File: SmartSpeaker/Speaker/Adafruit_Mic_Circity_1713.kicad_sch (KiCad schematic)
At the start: 17 parts, among them J2 HEADER-1X576MIL, Q1 CMA-4544PF-W

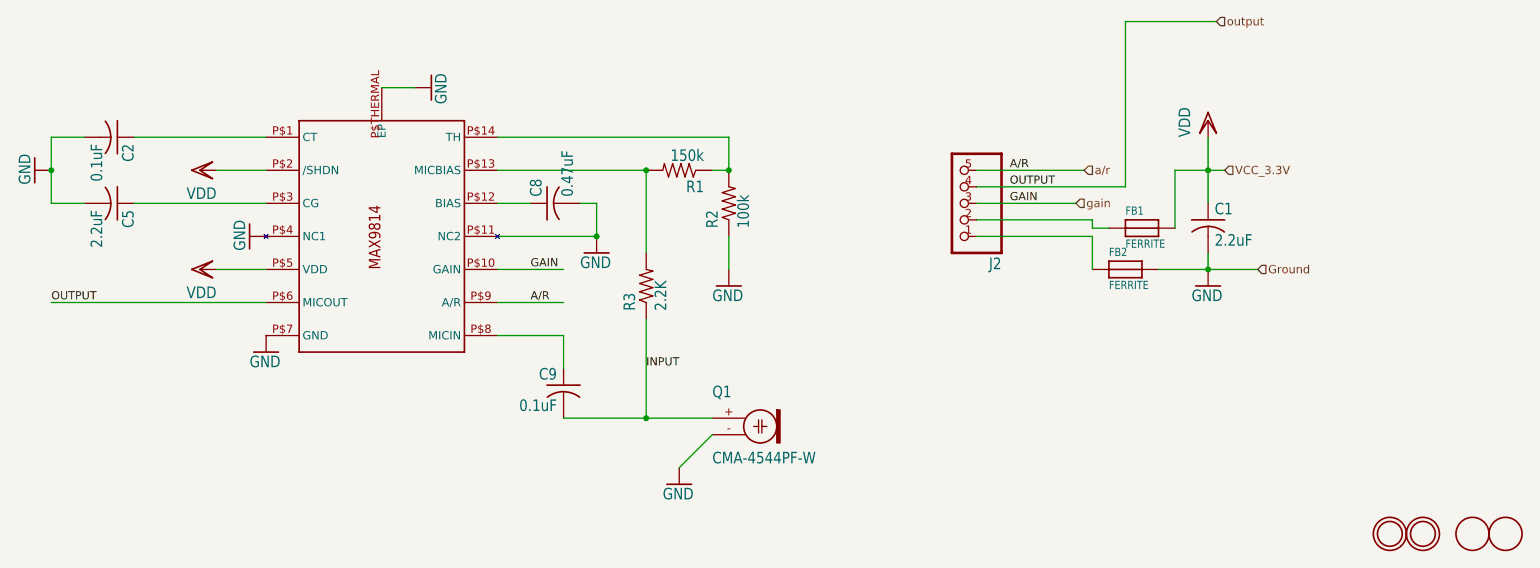
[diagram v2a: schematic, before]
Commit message: Fix some footprint problems, work towards a PCB
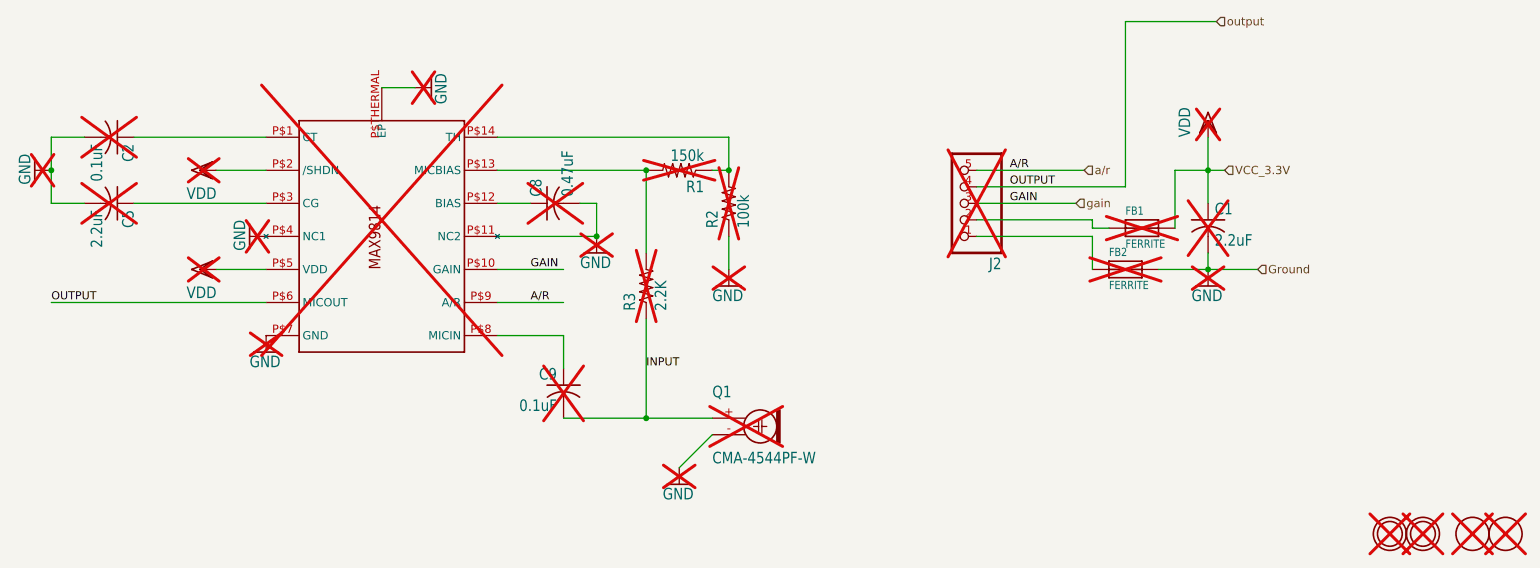
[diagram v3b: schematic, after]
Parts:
- C1, C2, C5, C8, C9, FB1, FB2, J2, Q1, R1, R2, R3, U$1, U$2, U$3, U$4, U$5: now not fitted
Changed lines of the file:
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@@
 		(in_bom yes)
 		(on_board no)
-		(dnp no)
+		(dnp yes)
 		(property "Reference" "R1"
 			(at 137.16 105.6386 0)
@@
 		(in_bom yes)
 		(on_board no)
-		(dnp no)
+		(dnp yes)
 		(property "Reference" "FB1"
 			(at 201.93 111.125 0)
@@
 		(in_bom yes)
 		(on_board no)
-		(dnp no)
+		(dnp yes)
 		(property "Reference" "#GND12"
 			(at 120.65 116.84 0)
@@
 		(in_bom yes)
 		(on_board no)
-		(dnp no)
+		(dnp yes)
 		(property "Reference" "R3"
 			(at 126.7714 125.73 0)
@@
 		(in_bom yes)
 		(on_board no)
-		(dnp no)
+		(dnp yes)
 		(property "Reference" "#GND9"
 			(at 140.97 121.92 0)
@@
 		(in_bom yes)
 		(on_board no)
-		(dnp no)
+		(dnp yes)
 		(property "Reference" "C1"
 			(at 215.646 111.125 0)
@@
 		(in_bom yes)
 		(on_board yes)
-		(dnp no)
+		(dnp yes)
 		(property "Reference" "#GND5"
 			(at 133.35 152.4 0)
@@
 		(in_bom yes)
 		(on_board no)
-		(dnp no)
+		(dnp yes)
 		(property "Reference" "#GND6"
 			(at 67.31 114.3 0)
@@
 		(in_bom yes)
 		(on_board no)
-		(dnp no)
+		(dnp yes)
 		(property "Reference" "R2"
 			(at 139.4714 113.03 0)
@@
 		(in_bom yes)
 		(on_board no)
-		(dnp no)
+		(dnp yes)
 		(property "Reference" "C8"
 			(at 112.395 108.204 0)
@@
 		(in_bom yes)
 		(on_board no)
-		(dnp no)
+		(dnp yes)
 		(property "Reference" "#GND2"
 			(at 95.25 91.44 0)
@@
 		(in_bom yes)
 		(on_board no)
-		(dnp no)
+		(dnp yes)
 		(property "Reference" "C5"
 			(at 47.625 110.236 0)
@@
 		(in_bom yes)
 		(on_board no)
-		(dnp no)
+		(dnp yes)
 		(property "Reference" "#VDD1"
 			(at 214.63 96.52 0)
@@
 		(in_bom yes)
 		(on_board no)
-		(dnp no)
+		(dnp yes)
 		(property "Reference" "J2"
 			(at 182.88 117.475 0)
@@
 		(in_bom yes)
 		(on_board no)
-		(dnp no)
+		(dnp yes)
 		(property "Reference" "#VDD8"
 			(at 59.69 119.38 0)
@@
 		(in_bom yes)
 		(on_board no)
-		(dnp no)
+		(dnp yes)
 		(property "Reference" "FB2"
 			(at 199.39 117.475 0)
@@
 		(in_bom yes)
 		(on_board no)
-		(dnp no)
+		(dnp yes)
 		(property "Reference" "U$1"
 			(at 85.09 134.62 0)
@@
 		(in_bom yes)
 		(on_board no)
-		(dnp no)
+		(dnp yes)
 		(property "Reference" "#VDD9"
 			(at 59.69 104.14 0)
@@
 		(in_bom yes)
 		(on_board no)
-		(dnp no)
+		(dnp yes)
 		(property "Reference" "Q1"
 			(at 138.43 137.16 0)
@@
 		(in_bom yes)
 		(on_board yes)
-		(dnp no)
+		(dnp yes)
 		(property "Reference" "#GND8"
 			(at 34.29 104.14 0)
@@
 		(in_bom yes)
 		(on_board no)
-		(dnp no)
+		(dnp yes)
 		(property "Reference" "#GND10"
 			(at 69.85 132.08 0)
@@
 		(in_bom yes)
 		(on_board yes)
-		(dnp no)
+		(dnp yes)
 		(property "Reference" "U$3"
 			(at 255.27 160.02 0)
@@
 		(in_bom yes)
 		(on_board no)
-		(dnp no)
+		(dnp yes)
 		(property "Reference" "C9"
 			(at 114.554 136.525 0)
@@
 		(in_bom yes)
 		(on_board yes)
-		(dnp no)
+		(dnp yes)
 		(property "Reference" "U$4"
 			(at 247.65 160.02 0)
@@
 		(in_bom yes)
 		(on_board yes)
-		(dnp no)
+		(dnp yes)
 		(property "Reference" "U$5"
 			(at 242.57 160.02 0)
@@
 		(in_bom yes)
 		(on_board no)
-		(dnp no)
+		(dnp yes)
 		(property "Reference" "#GND1"
 			(at 214.63 121.92 0)
@@
 		(in_bom yes)
 		(on_board yes)
-		(dnp no)
+		(dnp yes)
 		(property "Reference" "U$2"
 			(at 260.35 160.02 0)
@@
 		(in_bom yes)
 		(on_board no)
-		(dnp no)
+		(dnp yes)
 		(property "Reference" "C2"
 			(at 47.625 100.076 0)

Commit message: Edit PCB to fix issues: - Enlarge OSHW logo - Rotate footprints for screw terminals - Fix pad numbers for barrel jack
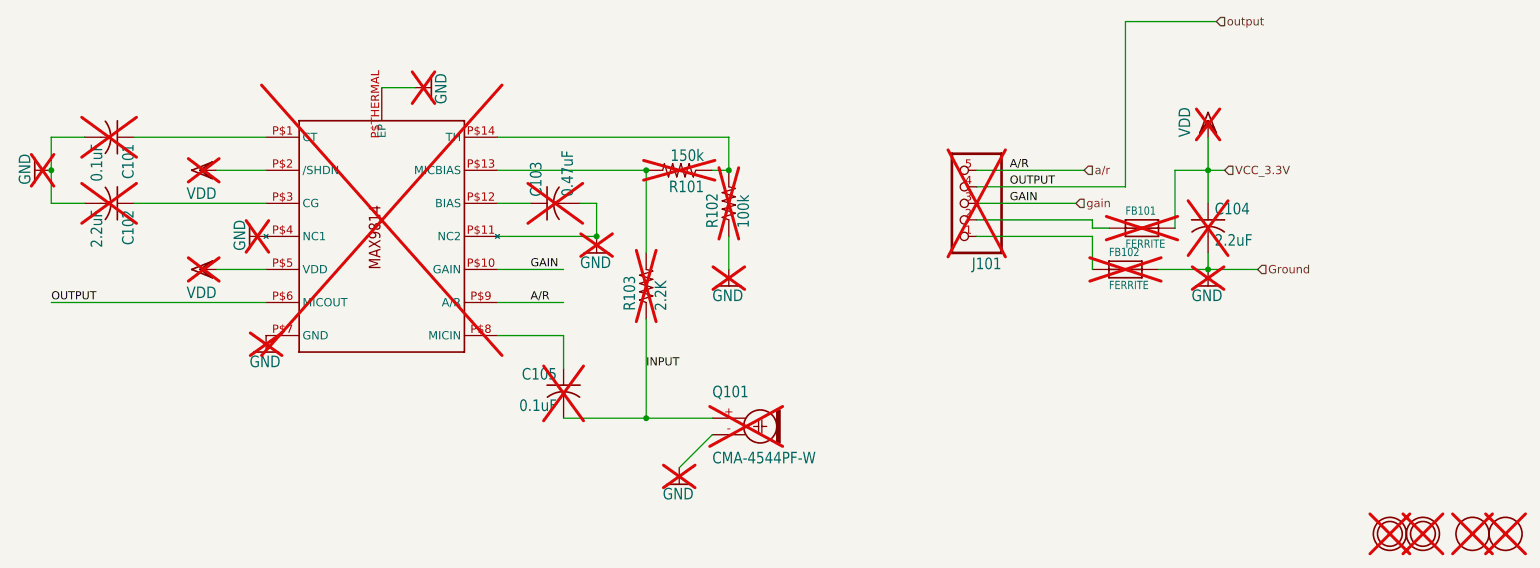
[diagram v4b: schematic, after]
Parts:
- renumbered C2 to C101, C5 to C102, C8 to C103, C1 to C104, C9 to C105, FB1 to FB101, FB2 to FB102, J2 to J101, Q1 to Q101, R1 to R101, R2 to R102, R3 to R103, U$1 to U$101, U$5 to U$102, U$4 to U$103, U$3 to U$104, U$2 to U$105
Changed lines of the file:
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@@
 (kicad_sch
-	(version 20231120)
+	(version 20250114)
 	(generator "eeschema")
-	(generator_version "8.0")
+	(generator_version "9.0")
 	(paper "A4")
 	(junction
@@
 		(on_board no)
 		(dnp yes)
-		(property "Reference" "R1"
+		(property "Reference" "R101"
 			(at 137.16 105.6386 0)
 			(effects
@@
 		(on_board no)
 		(dnp yes)
-		(property "Reference" "FB1"
+		(property "Reference" "FB101"
 			(at 201.93 111.125 0)
 			(effects
@@
 		(on_board no)
 		(dnp yes)
-		(property "Reference" "#GND12"
+		(property "Reference" "#GND0104"
 			(at 120.65 116.84 0)
 			(effects
@@
 		(on_board no)
 		(dnp yes)
-		(property "Reference" "R3"
+		(property "Reference" "R103"
 			(at 126.7714 125.73 0)
 			(effects
@@
 		(on_board no)
 		(dnp yes)
-		(property "Reference" "#GND9"
+		(property "Reference" "#GND0105"
 			(at 140.97 121.92 0)
 			(effects
@@
 		(on_board no)
 		(dnp yes)
-		(property "Reference" "C1"
+		(property "Reference" "C104"
 			(at 215.646 111.125 0)
 			(effects
@@
 		(on_board yes)
 		(dnp yes)
-		(property "Reference" "#GND5"
+		(property "Reference" "#GND0108"
 			(at 133.35 152.4 0)
 			(effects
@@
 		(on_board no)
 		(dnp yes)
-		(property "Reference" "#GND6"
+		(property "Reference" "#GND0103"
 			(at 67.31 114.3 0)
 			(effects
@@
 		(on_board no)
 		(dnp yes)
-		(property "Reference" "R2"
+		(property "Reference" "R102"
 			(at 139.4714 113.03 0)
 			(effects
@@
 		(on_board no)
 		(dnp yes)
-		(property "Reference" "C8"
+		(property "Reference" "C103"
 			(at 112.395 108.204 0)
 			(effects
@@
 		(on_board no)
 		(dnp yes)
-		(property "Reference" "#GND2"
+		(property "Reference" "#GND0101"
 			(at 95.25 91.44 0)
 			(effects
@@
 		(on_board no)
 		(dnp yes)
-		(property "Reference" "C5"
+		(property "Reference" "C102"
 			(at 47.625 110.236 0)
 			(effects
@@
 		(on_board no)
 		(dnp yes)
-		(property "Reference" "#VDD1"
+		(property "Reference" "#VDD0101"
 			(at 214.63 96.52 0)
 			(effects
@@
 		(on_board no)
 		(dnp yes)
-		(property "Reference" "J2"
+		(property "Reference" "J101"
 			(at 182.88 117.475 0)
 			(effects
@@
 		(on_board no)
 		(dnp yes)
-		(property "Reference" "#VDD8"
+		(property "Reference" "#VDD0103"
 			(at 59.69 119.38 0)
 			(effects
@@
 		(on_board no)
 		(dnp yes)
-		(property "Reference" "FB2"
+		(property "Reference" "FB102"
 			(at 199.39 117.475 0)
 			(effects
@@
 		(on_board no)
 		(dnp yes)
-		(property "Reference" "U$1"
+		(property "Reference" "U$101"
 			(at 85.09 134.62 0)
 			(effects
@@
 		(on_board no)
 		(dnp yes)
-		(property "Reference" "#VDD9"
+		(property "Reference" "#VDD0102"
 			(at 59.69 104.14 0)
 			(effects
@@
 		(on_board no)
 		(dnp yes)
-		(property "Reference" "Q1"
+		(property "Reference" "Q101"
 			(at 138.43 137.16 0)
 			(effects
@@
 		(on_board yes)
 		(dnp yes)
-		(property "Reference" "#GND8"
+		(property "Reference" "#GND0102"
 			(at 34.29 104.14 0)
 			(effects
@@
 		(on_board no)
 		(dnp yes)
-		(property "Reference" "#GND10"
+		(property "Reference" "#GND0107"
 			(at 69.85 132.08 0)
 			(effects
@@
 		(on_board yes)
 		(dnp yes)
-		(property "Reference" "U$3"
+		(property "Reference" "U$104"
 			(at 255.27 160.02 0)
 			(effects
@@
 		(on_board no)
 		(dnp yes)
-		(property "Reference" "C9"
+		(property "Reference" "C105"
 			(at 114.554 136.525 0)
 			(effects
@@
 		(on_board yes)
 		(dnp yes)
-		(property "Reference" "U$4"
+		(property "Reference" "U$103"
 			(at 247.65 160.02 0)
 			(effects
@@
 		(on_board yes)
 		(dnp yes)
-		(property "Reference" "U$5"
+		(property "Reference" "U$102"
 			(at 242.57 160.02 0)
 			(effects
@@
 		(on_board no)
 		(dnp yes)
-		(property "Reference" "#GND1"
+		(property "Reference" "#GND0106"
 			(at 214.63 121.92 0)
 			(effects
@@
 		(on_board yes)
 		(dnp yes)
-		(property "Reference" "U$2"
+		(property "Reference" "U$105"
 			(at 260.35 160.02 0)
 			(effects
@@
 		(on_board no)
 		(dnp yes)
-		(property "Reference" "C2"
+		(property "Reference" "C101"
 			(at 47.625 100.076 0)
 			(effects
